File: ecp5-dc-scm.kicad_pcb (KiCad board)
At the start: 6 copper layers, 90 x 120.4 mm, 147 parts, among them IC1 TPS54561, J1 WE-RJ45_7499111121A, J10 61300611121, J11 DC_SOCKET, J2 1-2199230-6, J3 543630489, J4 M20-7830642, J5 SFF-TA-1002-4C+, J6 2X05, J7 61301021121, J8 61301021121, J9 61301221121, U1 KSZ9031RNXCA, U14 ECP5UM5G_85_CABGA756, U2 W25Q32JVSSIQ_TR, U3 W25Q32JVSSIQ_TR, U4 W25Q32JVSSIQ_TR, U5 W25Q32JVSSIQ_TR, U6 NVT2008DQ,115, U7 AS4C256M16D3, U8 TPS51200DRC, Y1 ABM8G-25.000MHZ-18-D2Y-T

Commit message: Add local component libraries.
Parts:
- C1, C10, C11, C12, C13, C14, C15, C16, C17, C18, C19, C2, C20, C21, C22, C23, C24, C25, C26, C3, C35, C36, C37, C38, C4, C40, C41, C42, C43, C44, C45, C46, C47, C48, C49, C5, C50, C51, C52, C53, C54, C55, C56, C57, C58, C59, C6, C60, C61, C62, C63, C68, C69, C7, C70, C71, C8, C9: footprint antmicro-footprints:0402-cap -> ecp5-dc-scm-footprints:0402-cap
- C65, C66, C67, C72, C73, C74: footprint antmicro-footprints:0603-cap -> ecp5-dc-scm-footprints:0603-cap
- D2: footprint antmicro-footprints:PDS760-13 -> ecp5-dc-scm-footprints:PDS760-13
- F2: footprint antmicro-footprints:1206-Fuse-Littelfuse-0466-0-0-MFG -> ecp5-dc-scm-footprints:1206-Fuse-Littelfuse-0466-0-0-MFG
- FB1, FB2, FB3: footprint antmicro-footprints:0603-res -> ecp5-dc-scm-footprints:0603-res
- IC1: footprint antmicro-footprints:WSON-10_4x4 -> ecp5-dc-scm-footprints:WSON-10_4x4
- J1: footprint antmicro-footprints:7499111121A -> ecp5-dc-scm-footprints:7499111121A
- J10: footprint antmicro-footprints:61300611121 -> ecp5-dc-scm-footprints:61300611121
- J11: footprint antmicro-footprints:DC_SOCKET -> ecp5-dc-scm-footprints:DC_SOCKET
- J2: footprint antmicro-footprints:1-2199230-6 -> ecp5-dc-scm-footprints:1-2199230-6
- J3: footprint antmicro-footprints:543630489 -> ecp5-dc-scm-footprints:543630489
- J4: footprint antmicro-footprints:PinHeader_6x2_P2.54mm_Vertical -> ecp5-dc-scm-footprints:PinHeader_6x2_P2.54mm_Vertical
- J5: footprint antmicro-footprints:SFF-TA-1002-4C+ -> ecp5-dc-scm-footprints:SFF-TA-1002-4C+
- J6: footprint antmicro-footprints:SHF-105-01-X-D-SM -> ecp5-dc-scm-footprints:SHF-105-01-X-D-SM
- J7, J8: footprint antmicro-footprints:61301021121 -> ecp5-dc-scm-footprints:61301021121
- J9: footprint antmicro-footprints:61301221121 -> ecp5-dc-scm-footprints:61301221121
- L1: footprint antmicro-footprints:WE_7447798720 -> ecp5-dc-scm-footprints:WE_7447798720
- R1, R10, R11, R12, R13, R14, R2, R21, R22, R23, R24, R25, R26, R27, R28, R29, R3, R30, R31, R32, R33, R34, R35, R36, R37, R38, R39, R4, R40, R41, R42, R43, R44, R5, R57, R58, R59, R6, R60, R61, R62, R66, R67, R68, R69, R7, R70, R71, R72, R8, R9: footprint antmicro-footprints:0402-res -> ecp5-dc-scm-footprints:0402-res
- R54, R55, R56: footprint antmicro-footprints:R_Array_Convex_8x0602 -> ecp5-dc-scm-footprints:R_Array_Convex_8x0602
- TP1: footprint antmicro-footprints:Testpoint_smd_1mm -> ecp5-dc-scm-footprints:Testpoint_smd_1mm
- U1: footprint antmicro-footprints:QFN-48-Microchip-QFN77-48LD-PL-2 -> ecp5-dc-scm-footprints:QFN-48-Microchip-QFN77-48LD-PL-2
- U14: footprint antmicro-footprints:CABGA756_27x27mm_p0.8mm -> ecp5-dc-scm-footprints:CABGA756_27x27mm_p0.8mm
- U2, U3, U4, U5: footprint antmicro-footprints:W25Q32JVSSIQ -> ecp5-dc-scm-footprints:W25Q32JVSSIQ
- U6: footprint antmicro-footprints:QFN50P250X450X100-21N -> ecp5-dc-scm-footprints:QFN50P250X450X100-21N
- U7: footprint antmicro-footprints:BGA-96_9.0x13.0mm_Layout2x3x16_P0.8mm -> ecp5-dc-scm-footprints:BGA-96_9.0x13.0mm_Layout2x3x16_P0.8mm
- U8: footprint antmicro-footprints:VSON-10-1EP_3x3mm -> ecp5-dc-scm-footprints:VSON-10-1EP_3x3mm
- Y1: footprint antmicro-footprints:KX-7 -> ecp5-dc-scm-footprints:KX-7

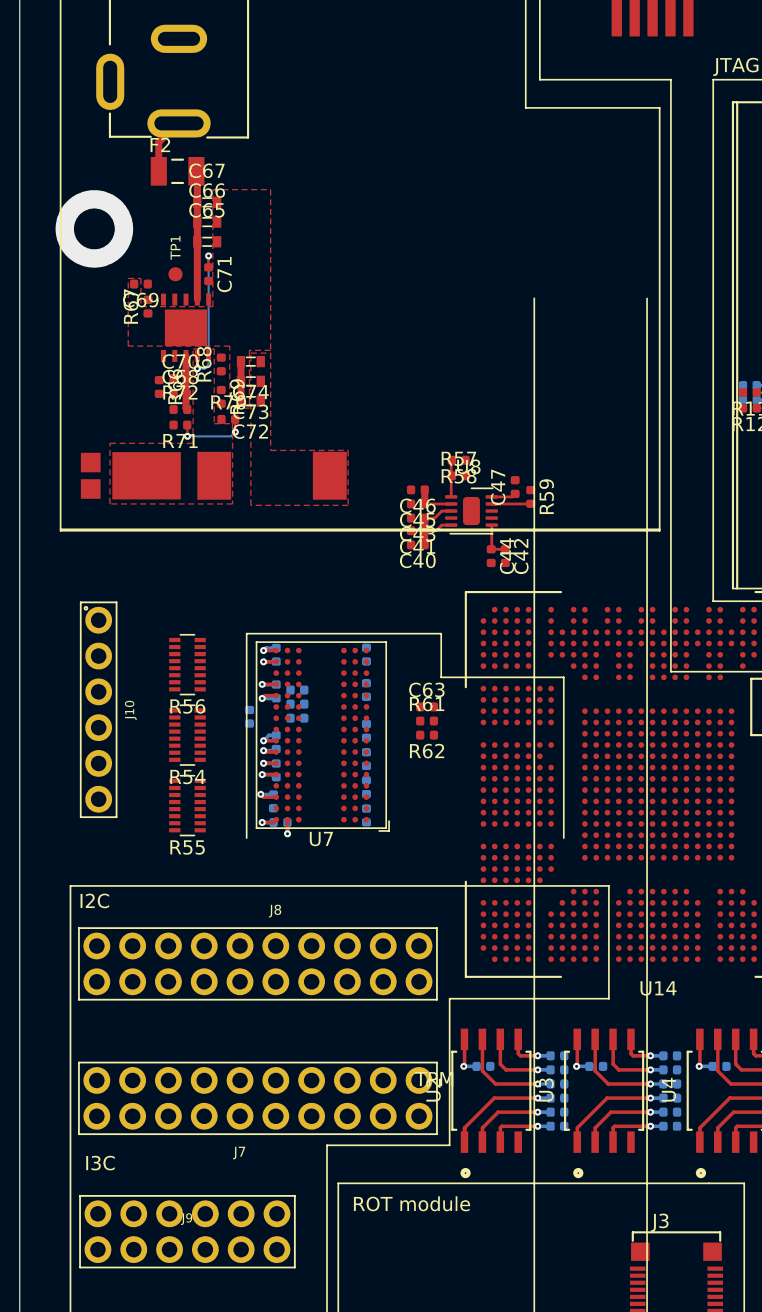
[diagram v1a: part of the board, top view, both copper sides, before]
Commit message: Add power supply placement and initial routing
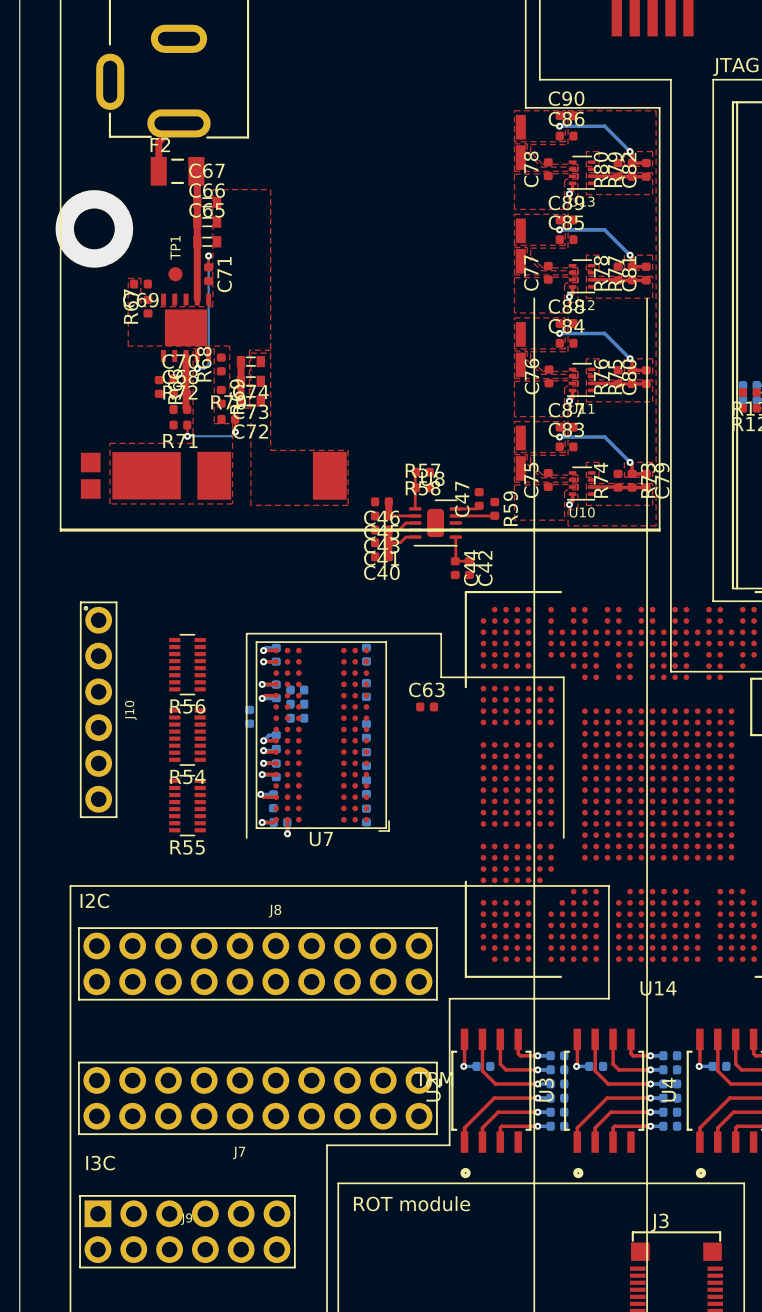
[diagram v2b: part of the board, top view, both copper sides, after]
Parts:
- removed R61, R62: R_51R_0402, ecp5-dc-scm-footprints:0402-res
- added C75: C_10u_0402, ecp5-dc-scm-footprints:0402-cap, F.Cu at (97.6, 97.9)
- added C76: C_10u_0402, ecp5-dc-scm-footprints:0402-cap, F.Cu at (97.7, 90.5)
- added C77: C_10u_0402, ecp5-dc-scm-footprints:0402-cap, F.Cu at (97.6, 83.2)
- added C78: C_10u_0402, ecp5-dc-scm-footprints:0402-cap, F.Cu at (97.6, 75.8)
- added C79: C_120p_0402, ecp5-dc-scm-footprints:0402-res, F.Cu at (104.5, 98.0)
- added C80: C_120p_0402, ecp5-dc-scm-footprints:0402-res, F.Cu at (104.5, 90.6)
- added C81: C_120p_0402, ecp5-dc-scm-footprints:0402-res, F.Cu at (104.5, 83.2)
- added C82: C_120p_0402, ecp5-dc-scm-footprints:0402-res, F.Cu at (104.5, 75.9)
- added C83: C_10u_0402, ecp5-dc-scm-footprints:0402-cap, F.Cu at (98.9, 95.5)
- added C84: C_10u_0402, ecp5-dc-scm-footprints:0402-cap, F.Cu at (98.9, 88.2)
- added C85: C_10u_0402, ecp5-dc-scm-footprints:0402-cap, F.Cu at (98.9, 80.8)
- added C86: C_10u_0402, ecp5-dc-scm-footprints:0402-cap, F.Cu at (98.9, 73.5)
- added C87: C_10u_0402, ecp5-dc-scm-footprints:0402-cap, F.Cu at (98.9, 94.2)
- added C88: C_10u_0402, ecp5-dc-scm-footprints:0402-cap, F.Cu at (98.9, 86.8)
- added C89: C_10u_0402, ecp5-dc-scm-footprints:0402-cap, F.Cu at (98.9, 79.5)
- added C90: C_10u_0402, ecp5-dc-scm-footprints:0402-cap, F.Cu at (98.9, 72.0)
- added L2: IHLP1212AEERR47M11, ecp5-dc-scm-footprints:IHLP-1212AE, F.Cu at (95.7, 96.0)
- added L3: IHLP1212AEERR47M11, ecp5-dc-scm-footprints:IHLP-1212AE, F.Cu at (95.7, 88.7)
- added L4: IHLP1212AEERR47M11, ecp5-dc-scm-footprints:IHLP-1212AE, F.Cu at (95.7, 81.3)
- added L5: IHLP1212AEERR47M11, ecp5-dc-scm-footprints:IHLP-1212AE, F.Cu at (95.7, 74.0)
- added R73: R_453k_0402, ecp5-dc-scm-footprints:0402-res, F.Cu at (103.5, 98.0)
- added R74: R_100k_0402, ecp5-dc-scm-footprints:0402-res, F.Cu at (102.5, 98.0)
- added R75: R_200k_0402, ecp5-dc-scm-footprints:0402-res, F.Cu at (103.5, 90.6)
- added R76: R_100k_0402, ecp5-dc-scm-footprints:0402-res, F.Cu at (102.5, 90.6)
- added R77: R_124k_0402, ecp5-dc-scm-footprints:0402-res, F.Cu at (103.5, 83.2)
- added R78: R_100k_0402, ecp5-dc-scm-footprints:0402-res, F.Cu at (102.5, 83.2)
- added R79: R_124k_0402, ecp5-dc-scm-footprints:0402-res, F.Cu at (103.5, 75.9)
- added R80: R_100k_0402, ecp5-dc-scm-footprints:0402-res, F.Cu at (102.5, 75.9)
- added U10: TPS62823DLCT, ecp5-dc-scm-footprints:QFN-8_2x1mm, F.Cu at (100.0, 98.2)
- added U11: TPS62823DLCT, ecp5-dc-scm-footprints:QFN-8_2x1mm, F.Cu at (100.0, 90.8)
- added U12: TPS62823DLCT, ecp5-dc-scm-footprints:QFN-8_2x1mm, F.Cu at (100.0, 83.5)
- added U13: TPS62823DLCT, ecp5-dc-scm-footprints:QFN-8_2x1mm, F.Cu at (100.0, 76.1)
- moved C42 2.69 mm to (92.0, 104.2)
- moved C43 2.69 mm to (85.8, 101.5)
- moved C44 2.69 mm to (91.0, 104.2)
- moved C45 2.69 mm to (85.8, 100.5)
- moved C46 2.69 mm to (85.8, 99.5)
- moved R57 2.69 mm to (88.7, 98.5)
- moved R59 2.69 mm to (93.8, 100.0)
- moved U8 2.69 mm to (89.4, 101.2)
- moved C40 2.69 mm to (85.8, 103.3)
- moved C41 2.69 mm to (85.8, 102.3)
- moved C47 2.69 mm to (92.7, 99.2)
- moved R58 2.69 mm to (88.7, 97.3)
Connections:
- J2 pad 17: Net-(J2-Pad17) -> PCIE_HPM_RXN[2]
- J2 pad 19: Net-(J2-Pad19) -> PCIE_HPM_RXP[2]
- J2 pad 29: Net-(J2-Pad29) -> PCIE_HPM_RXN[1]
- J2 pad 31: Net-(J2-Pad31) -> PCIE_HPM_RXP[1]
- J2 pad 5: Net-(J2-Pad5) -> PCIE_HPM_RXN[3]
- J2 pad 7: Net-(J2-Pad7) -> PCIE_HPM_RXP[3]
- U14 pad L27: Net-(U14-PadL27) -> PCIE_BMC_RX_DP
- U14 pad N26: Net-(U14-PadN26) -> CLK_100M_PCIE_DN
- U14 pad N27: Net-(U14-PadN27) -> PCIE_BMC_TX_DN
- U14 pad N29: Net-(U14-PadN29) -> PCIE_BMC_RX_DN
- U14 pad P26: Net-(U14-PadP26) -> CLK_100M_PCIE_DP
- U14 pad P27: Net-(U14-PadP27) -> PCIE_BMC_TX_DP
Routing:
- net (no net): track 10.0 -> 21.7 mm
- net VCC3V3: track 20.1 -> 27.7 mm, vias 7 -> 9
- net Net-(C82-Pad2): track 0.00 -> 7.62 mm, vias 0 -> 2
- net Net-(C81-Pad2): track 0.00 -> 7.62 mm, vias 0 -> 2
- net Net-(C80-Pad2): track 0.00 -> 7.62 mm, vias 0 -> 2
- net Net-(C79-Pad2): track 0.00 -> 3.89 mm
- net /Power supply/1V8_PG: track 0.00 -> 0.84 mm, vias 0 -> 1
- net /Power supply/1V35_PG: track 0.00 -> 0.84 mm, vias 0 -> 1
- net /Power supply/3V3_PG: track 0.00 -> 0.84 mm, vias 0 -> 1
- net /Power supply/1V0_PG: track 0.00 -> 0.84 mm, vias 0 -> 1
- added copper zone on F.Cu, net Net-(L2-Pad1)
- added copper zone on F.Cu, net Net-(L3-Pad1)
- added copper zone on F.Cu, net Net-(L4-Pad1)
- added copper zone on F.Cu, net Net-(L5-Pad1)
- added copper zone on F.Cu, net VCC1V0
- added copper zone on F.Cu, net VCC1V35
- added copper zone on F.Cu, net VCC1V8
- added copper zone on F.Cu, net VCC3V3
- added copper zone on F.Cu, net VCC5V0

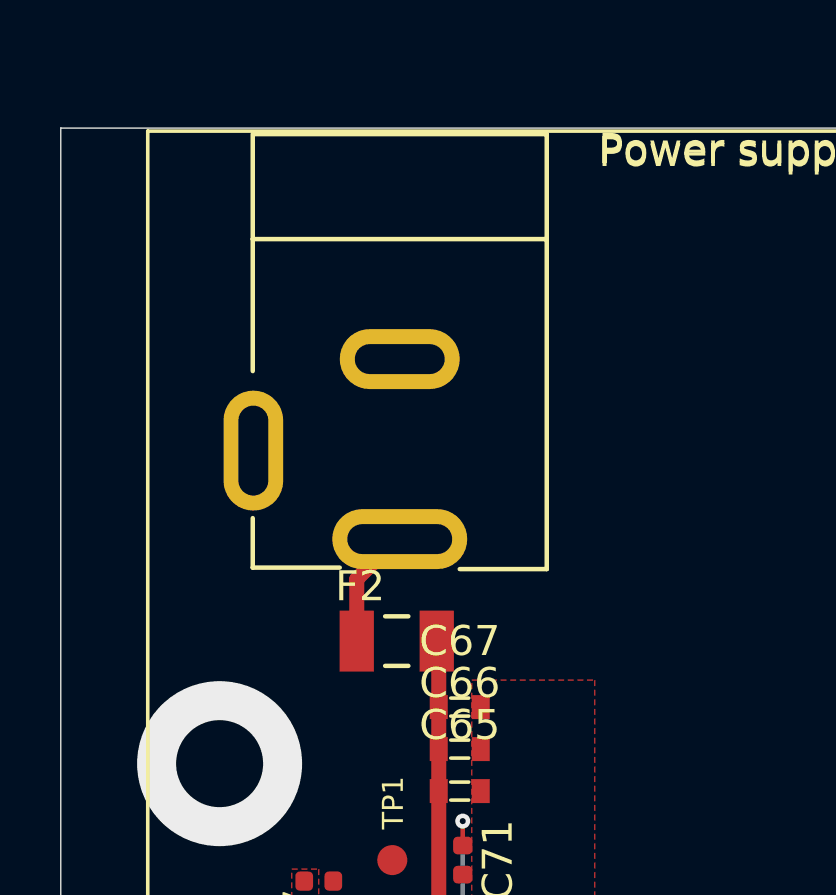
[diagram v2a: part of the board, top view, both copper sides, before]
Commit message: Remove DC jack connector
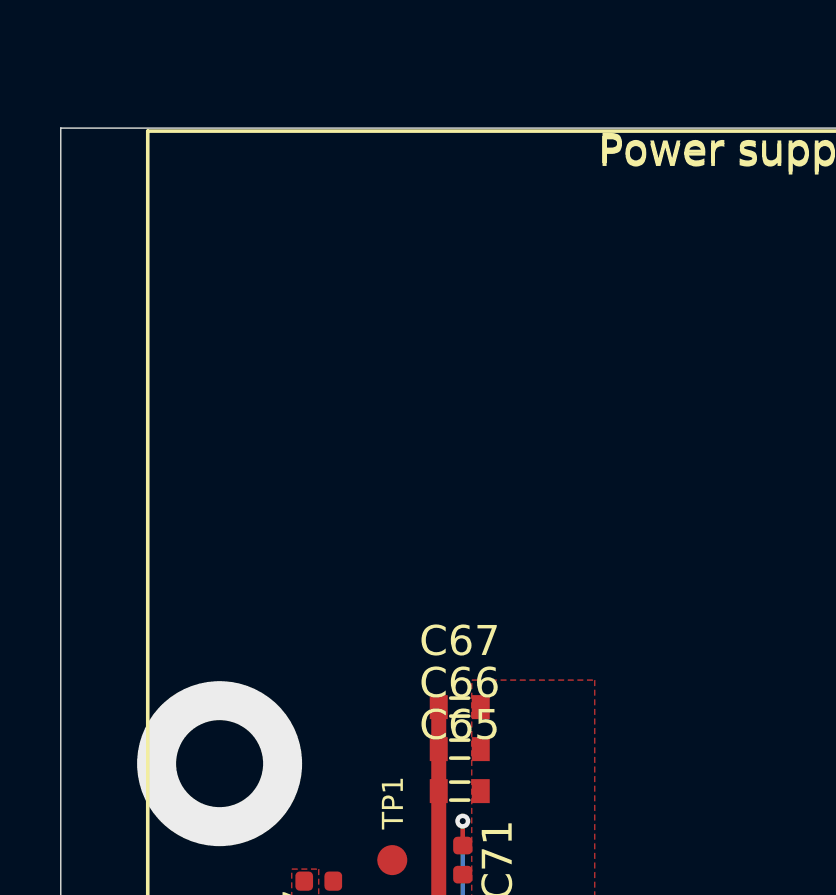
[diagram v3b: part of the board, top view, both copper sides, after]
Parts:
- removed F2: 0466003.NR, ecp5-dc-scm-footprints:1206-Fuse-Littelfuse-0466-0-0-MFG
- removed J11: DC_SOCKET, ecp5-dc-scm-footprints:DC_SOCKET
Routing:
- net Net-(F2-Pad1): track 4.09 -> 0.00 mm
- net (no net): track 21.7 -> 19.5 mm

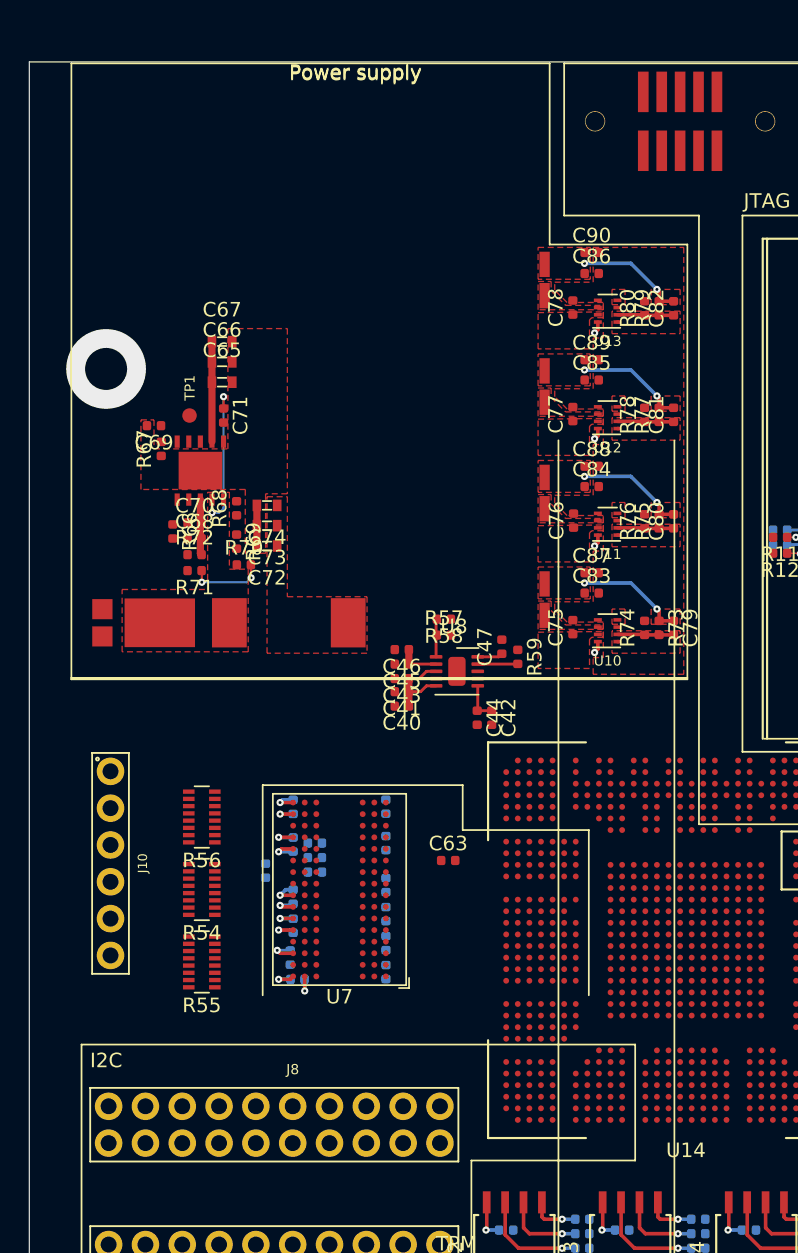
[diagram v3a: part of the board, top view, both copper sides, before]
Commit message: 1v2 power supply component placement
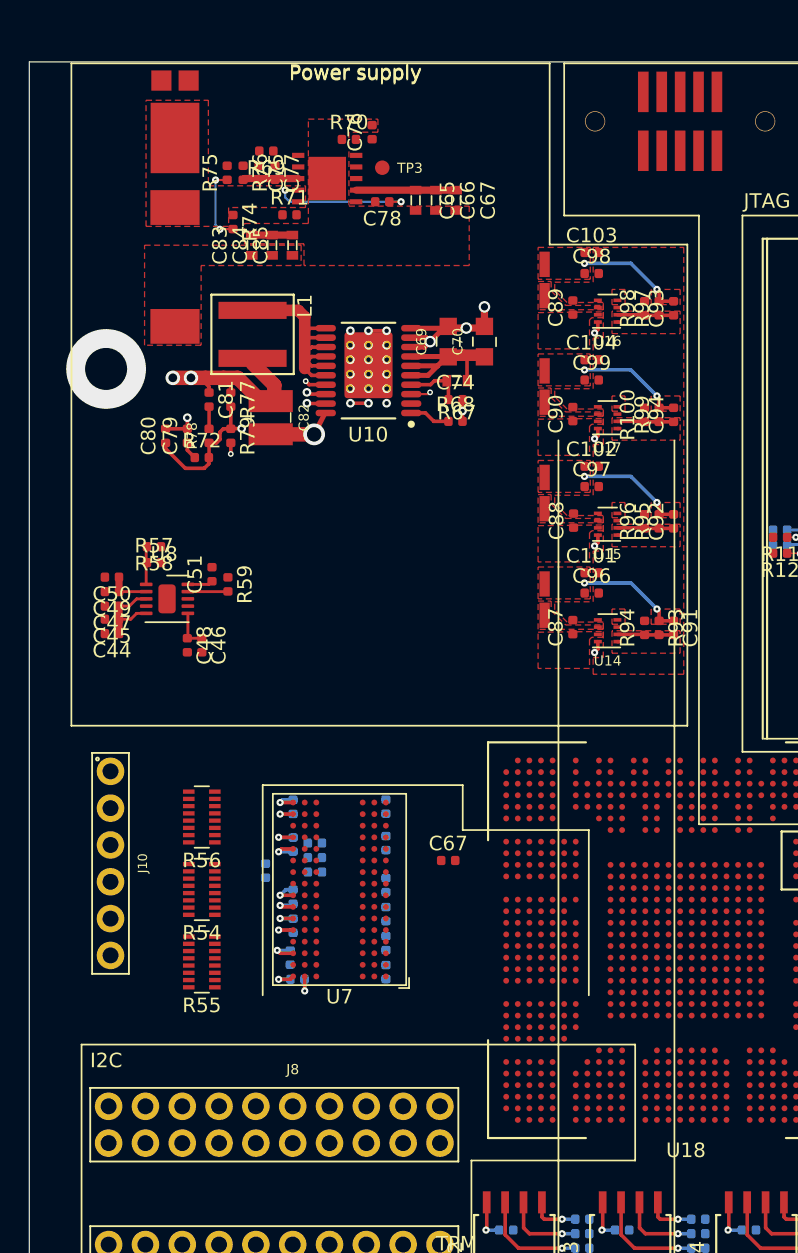
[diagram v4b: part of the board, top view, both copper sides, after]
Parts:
- removed the R69 at (74.4, 92.0)
- added C69: C_10u_0805, antmicro-footprints:0805-cap, F.Cu at (89.0, 78.2)
- added C70: C_10u_0805, antmicro-footprints:0805-cap, F.Cu at (91.5, 78.2)
- added C74: C_100n_0402, ecp5-dc-scm-footprints:0402-cap, F.Cu at (89.5, 82.2)
- added C79: C_1n8_0402, ecp5-dc-scm-footprints:0402-cap, F.Cu at (71.0, 84.7)
- added C80: C_180p_0402, ecp5-dc-scm-footprints:0402-cap, F.Cu at (69.5, 84.7)
- added C81: C_750p_0402, ecp5-dc-scm-footprints:0402-res, F.Cu at (72.5, 82.2)
- added C82: C_47u_1210, antmicro-footprints:1210-cap, F.Cu at (76.8, 83.5)
- added L1: XAL5030-801, ecp5-dc-scm-footprints:Coilcraft-XAL5030, F.Cu at (75.5, 77.7)
- added R67: R_10R_0603, ecp5-dc-scm-footprints:0603-res, F.Cu at (89.6, 80.9)
- added R68: R_47k_0402, ecp5-dc-scm-footprints:0402-res, F.Cu at (89.5, 83.7)
- added R72: R_4k7_0402, ecp5-dc-scm-footprints:0402-res, F.Cu at (72.0, 86.2)
- added R77: R_10k_0402, ecp5-dc-scm-footprints:0402-res, F.Cu at (74.0, 82.2)
- added R78: R_470k_0402, antmicro-footprints:0402-res, F.Cu at (72.5, 84.7)
- added R79: R_10k_0402, ecp5-dc-scm-footprints:0402-res, F.Cu at (74.0, 84.7)
- added U10: LM21212-2, ecp5-dc-scm-footprints:HTSSOP-20_TI-PWP, F.Cu at (83.5, 80.2)
- moved D2 34.1 mm to (70.0, 63.6), turned to 90 degrees
- moved R75 27.5 mm to (73.8, 66.5), turned to 90 degrees
- moved R69 27.0 mm to (76.5, 65.0), turned to 180 degrees
- moved R76 26.6 mm to (74.8, 66.5), turned to 270 degrees
- moved L2 25.8 mm to (70.2, 73.0), turned to 270 degrees
- moved C75 25.6 mm to (76.0, 66.5), turned to 270 degrees
- moved C76 25.2 mm to (83.8, 63.8), turned to 90 degrees
- moved R70 25.0 mm to (82.2, 64.2), turned to 0 degrees
- moved C77 24.8 mm to (77.0, 66.5), turned to 270 degrees
- moved R74 23.7 mm to (74.2, 70.0), turned to 270 degrees
- moved IC1 22.0 mm to (80.7, 67.0), turned to 180 degrees
- moved TP3 21.7 mm to (84.5, 66.2), turned to 180 degrees
- moved C83 20.8 mm to (75.5, 71.5), turned to 90 degrees
- moved C44 20.6 mm to (65.8, 98.3)
- moved C45 20.6 mm to (65.8, 97.3)
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- renumbered C87 to C101, C88 to C102, C90 to C103, C89 to C104, C35 to C39, C36 to C40, C37 to C41, C38 to C42, C40 to C44, C41 to C45, C42 to C46, C43 to C47, C44 to C48, C45 to C49, C46 to C50, C47 to C51, C48 to C52, C49 to C53, C50 to C54, C51 to C55, C52 to C56, C53 to C57, C54 to C58, C55 to C59, C56 to C60, C57 to C61, C58 to C62, C59 to C63, C60 to C64, C61 to C65, C62 to C66, C63 to C67, C68 to C75, C69 to C76, C70 to C77, C71 to C78, C72 to C83, C73 to C84, C74 to C85, C75 to C87, C76 to C88, C78 to C89, C77 to C90, C79 to C91, C80 to C92, C82 to C93, C81 to C94, C83 to C96, C84 to C97, C86 to C98, C85 to C99, L1 to L2, L2 to L3, L3 to L4, L4 to L6, R78 to R100, R66 to R69, R67 to R70, R68 to R71, R70 to R74, R71 to R75, R72 to R76, R73 to R93, R74 to R94, R75 to R95, R76 to R96, R79 to R97, R80 to R98, R77 to R99, TP1 to TP3, U10 to U14, U11 to U15, U13 to U16, U12 to U17, U14 to U18
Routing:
- net GND: track 19.7 -> 37.7 mm, vias 5 -> 11
- net Net-(L1-Pad1): track 0.00 -> 16.6 mm
- net (no net): track 19.5 -> 32.5 mm, vias 2 -> 20
- net +1V2: track 0.00 -> 12.6 mm, vias 0 -> 2
- net VCC5V0: track 0.30 -> 12.1 mm
- net Net-(C80-Pad1): track 0.00 -> 11.3 mm, vias 0 -> 2
- net Net-(C74-Pad1): track 0.00 -> 3.98 mm
- net Net-(C79-Pad2): track 0.00 -> 3.61 mm, vias 0 -> 2
- net Net-(R68-Pad1): track 0.00 -> 2.81 mm
- net Net-(C81-Pad2): track 0.00 -> 1.53 mm
- net /Power supply/1V2_PG: track 0.00 -> 1.48 mm, vias 0 -> 1
- net /Power supply/1V2_EN: track 0.00 -> 1.35 mm, vias 0 -> 1
- net Net-(C79-Pad1): track 0.00 -> 1.23 mm
- removed copper zone on F.Cu, net Net-(L6-Pad1)
